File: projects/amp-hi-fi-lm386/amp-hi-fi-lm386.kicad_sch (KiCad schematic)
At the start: 11 parts, among them J1 AudioJack, U1 LM386

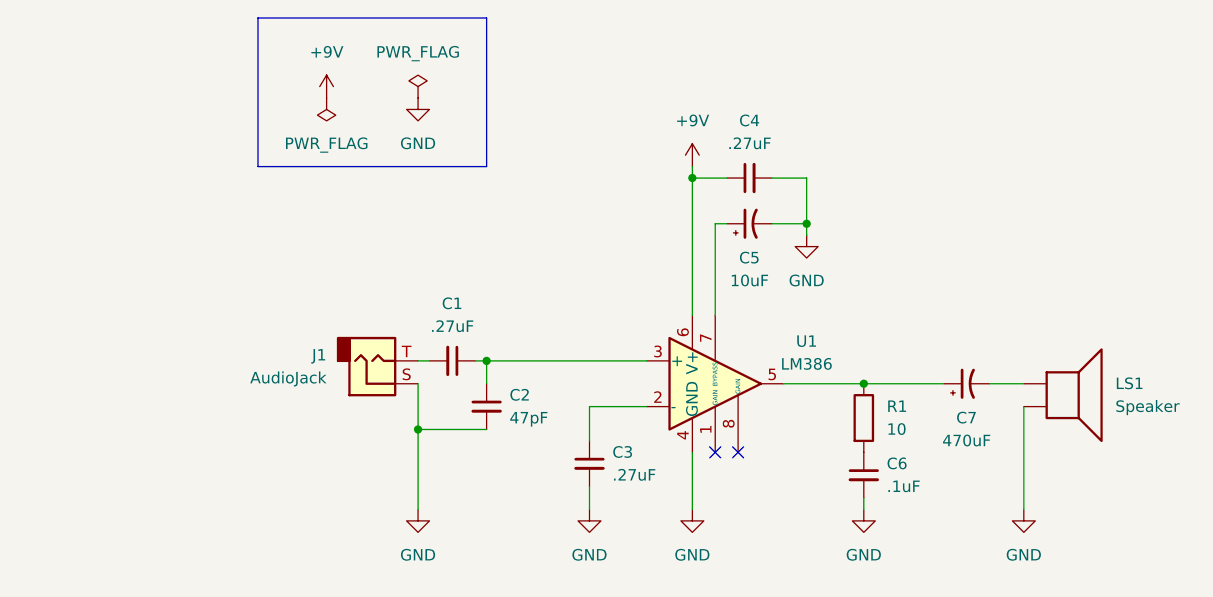
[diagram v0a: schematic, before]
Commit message: Initial checkin of l386 amp with bass boost
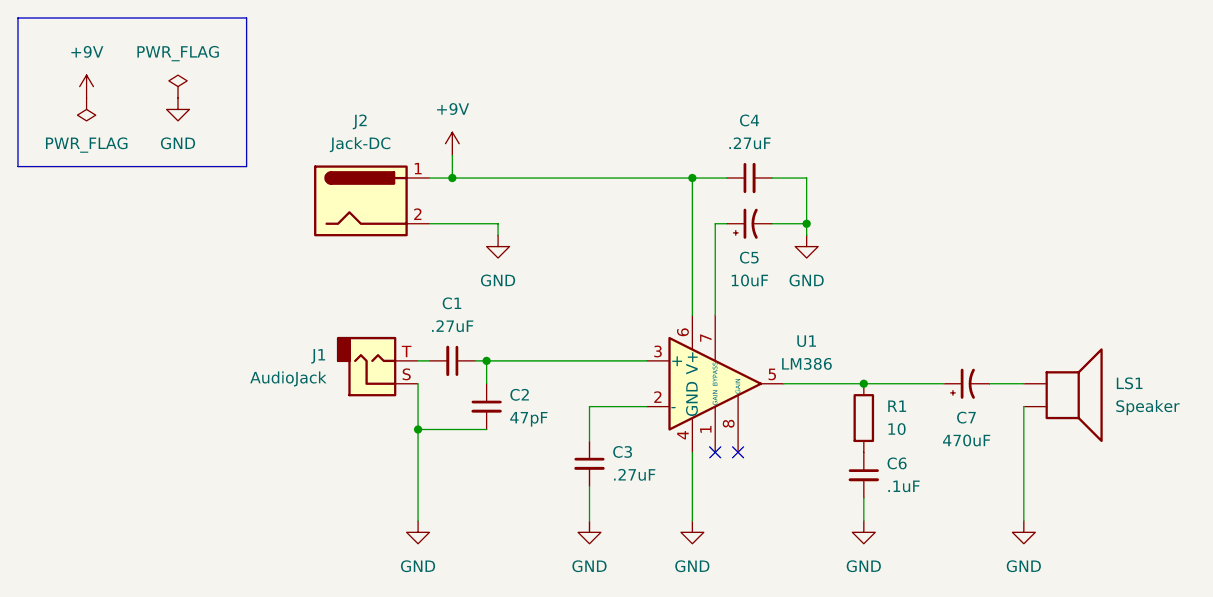
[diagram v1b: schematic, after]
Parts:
- added J2: Jack-DC, Connector_PinHeader_2.54mm:PinHeader_1x02_P2.54mm_Vertical, symbol Connector:Jack-DC
- C1, C2, C3, C4, C5, C6, C7: footprint (none) -> Capacitor_THT:CP_Axial_L10.0mm_D4.5mm_P15.00mm_Horizontal
- J1: footprint (none) -> jme-audio-pinheader-2.54-vertical
- LS1: footprint (none) -> Connector_PinHeader_2.54mm:PinHeader_1x02_P2.54mm_Vertical
- R1: footprint (none) -> Resistor_THT:R_Axial_DIN0414_L11.9mm_D4.5mm_P20.32mm_Horizontal
- U1: footprint (none) -> LM386:DIP08
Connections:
- net +9V: now also J2.1
- net GND: now also J2.2
